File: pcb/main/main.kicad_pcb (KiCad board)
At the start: 2 copper layers, 82 x 44 mm, 46 parts, among them J1 USB_B_Micro, J2 Conn_01x12, J3 ISP, J4 Conn_01x12, Q1 DMP3099L, SW1 SW_Push, U1 CH340G, U2 TLV70033, U3 ATmega328P-AU, U4 RFM95W-915S2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

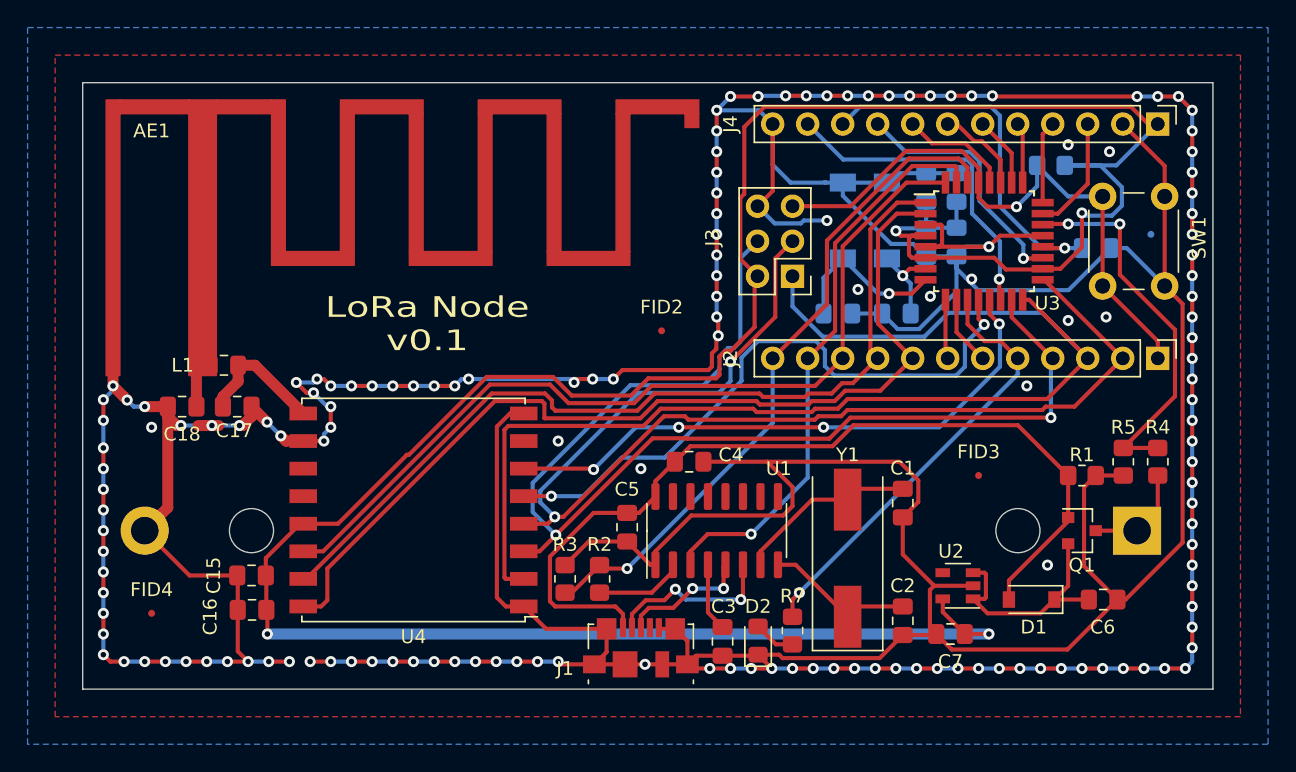
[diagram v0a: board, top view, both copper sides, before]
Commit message: Fix fiducials and annotations
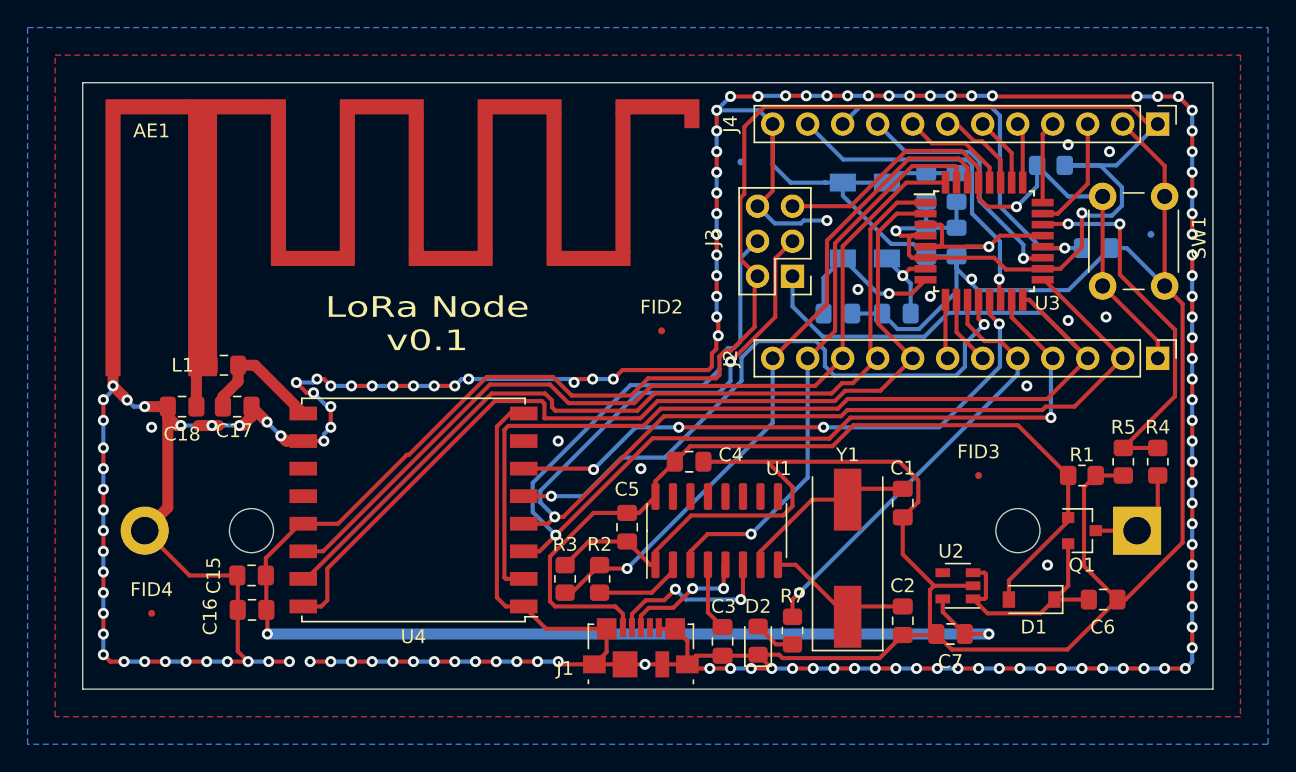
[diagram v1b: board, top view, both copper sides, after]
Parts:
- added FID5: Fiducial, Fiducial:Fiducial_0.5mm_Mask1.5mm, B.Cu at (150.8, 77.8)
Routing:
- net GND: vias 154 -> 153
- net (no net): vias 0 -> 1
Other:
- board text added: "Fabricante MAYER: Ancho de pista: 0,3mm y 0,8mm Vias: 0.8mm/0,4mm Margen global: 0,25mm Terminacion: HASL Grillas: 0.5mm y 0.25mm posicionamiento 0.25mm ruteo"
- board text removed: "Fabricante MAYER: Ancho de pista: 0,3mm y 0,8mm Vias: 1,6mm/0,8mm Margen global: 0,25mm Terminacion: HASL Grillas: 0.5mm y 0.25mm posicionamiento 0.25mm ruteo"

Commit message: Correcciones
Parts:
- moved FID3 17.3 mm to (180.5, 112.5)
- moved J1 0.35 mm to (143.5, 113.3)
- moved FID5 0.25 mm to (151.0, 77.8)
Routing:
- net /D3: track 64.2 -> 65.1 mm
- net /MISO: track 89.7 -> 90.3 mm, vias 0 -> 2
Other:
- board text added: "Diseñado en Argentina"
